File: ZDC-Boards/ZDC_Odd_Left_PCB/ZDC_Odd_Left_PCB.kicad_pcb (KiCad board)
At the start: 2 copper layers, 178.2 x 643 mm, 72 parts

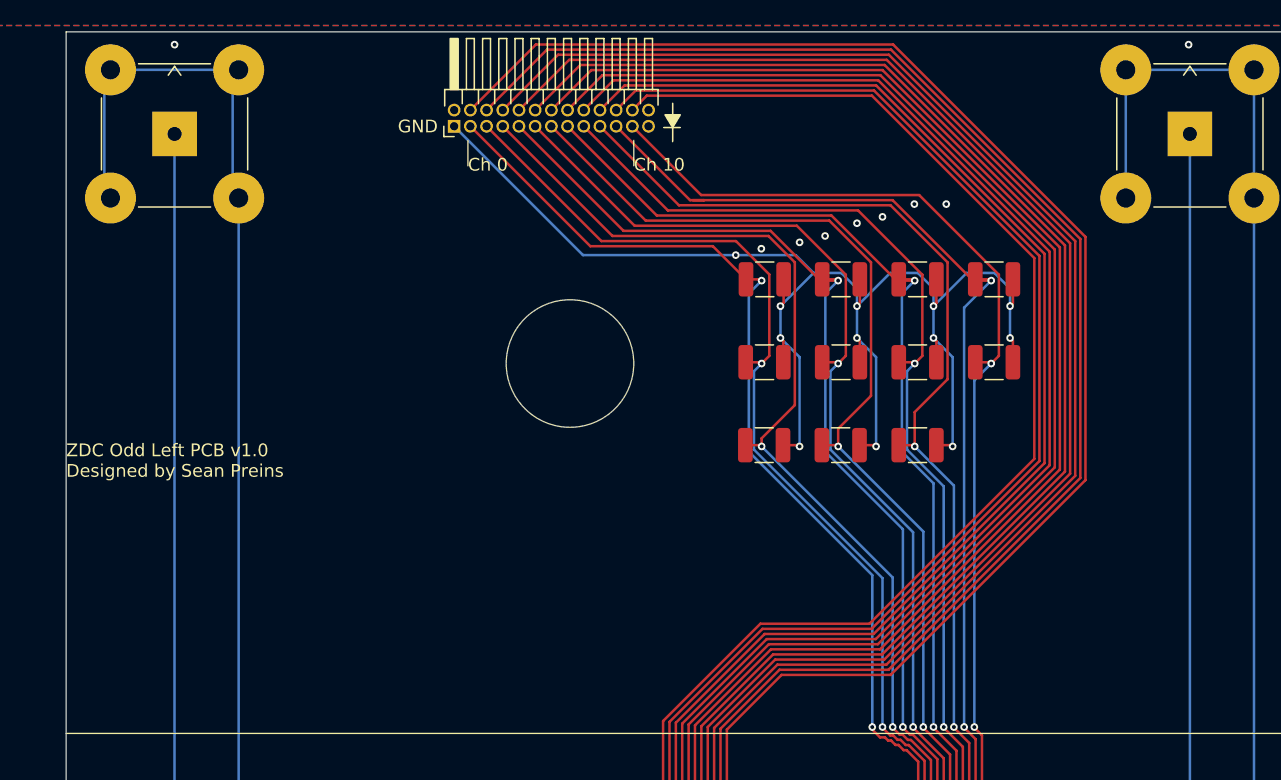
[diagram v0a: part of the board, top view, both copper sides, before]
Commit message: Updated small connector on ZDC PCBs
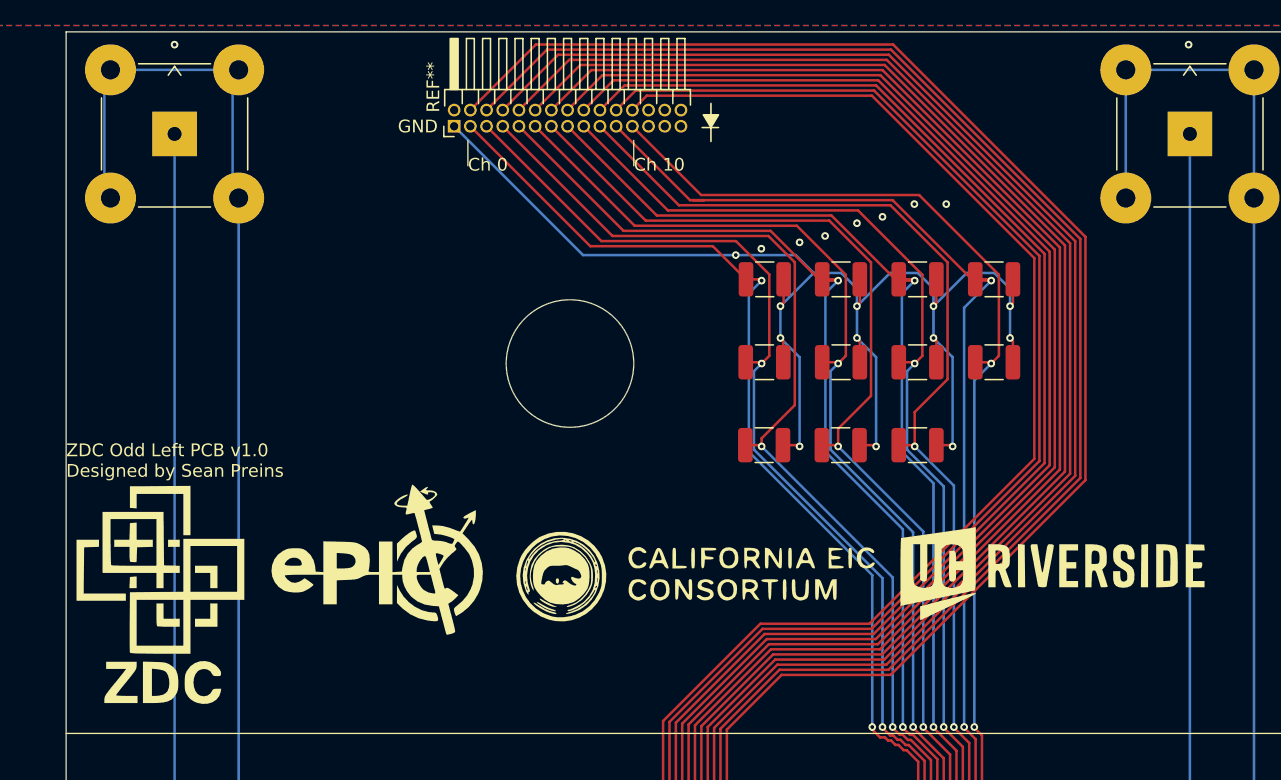
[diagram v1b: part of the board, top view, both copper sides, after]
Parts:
- removed the REF** at (47.4, -635.6)
- added G***: LOGO, LOGO, F.Cu at (62.0, -599.0)
- added REF**: PinHeader_2x15_P1.27mm_Horizontal, Connector_PinHeader_1.27mm:PinHeader_2x15_P1.27mm_Horizontal, F.Cu at (47.4, -635.6)
- moved REF**20 3.00 mm to (67.5, -635.5)
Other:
- board text removed: "PinHeader_2x13_P1.27mm_Horizontal"
